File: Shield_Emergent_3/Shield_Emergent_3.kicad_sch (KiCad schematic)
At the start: 17 parts, among them J1 USB3_B_Micro, J2 Conn_02x04_Odd_Even, J3 USB3_B_Micro, U3 SP3012-06UTG, U4 SP3012-06UTG, X1 USB_C_24pins

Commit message: v1.1 Geometry was established, LF routing was completed
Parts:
- removed J2: Conn_02x04_Odd_Even, Connector_PinHeader_2.54mm:PinHeader_2x04_P2.54mm_Vertical, symbol Connector_Generic:Conn_02x04_Odd_Even
- added J2: Conn_02x03_Odd_Even, Connector_PinSocket_2.54mm:PinSocket_2x03_P2.54mm_Vertical, symbol Connector_Generic:Conn_02x03_Odd_Even
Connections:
- net BTN1: now also J2.5 (Pin_5)
- net BTN2: now also J2.6 (Pin_6)
- net EN1: now also J2.1 (Pin_1)
- net EN2: now also J2.2 (Pin_2)
- net nFLT1: now also J2.3 (Pin_3)
- net nFLT2: now also J2.4 (Pin_4)
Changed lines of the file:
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@@
 	(wire
 		(pts
-			(xy 50.8 33.02) (xy 52.07 33.02)
-		)
-		(stroke
-			(width 0)
-			(type default)
-		)
-	)
-	(wire
-		(pts
 			(xy 234.95 53.34) (xy 236.22 53.34)
 		)
@@
 	(wire
 		(pts
-			(xy 36.83 33.02) (xy 38.1 33.02)
-		)
-		(stroke
-			(width 0)
-			(type default)
-		)
-	)
-	(wire
-		(pts
 			(xy 66.04 67.31) (xy 68.58 67.31)
 		)
@@
 		)
 	)
-	(global_label "VOUT2"
-		(shape input)
-		(at 52.07 33.02 0)
-		(fields_autoplaced yes)
-		(effects
-			(font
-				(size 1.27 1.27)
-			)
-			(justify left)
-		)
-		(property "Intersheetrefs" "${INTERSHEET_REFS}"
-			(at 60.9819 33.02 0)
-			(effects
-				(font
-					(size 1.27 1.27)
-				)
-				(justify left)
-				(hide yes)
-			)
-		)
-	)
 	(global_label "RX2+"
 		(shape input)
@@
 		)
 	)
-	(global_label "VOUT1"
-		(shape input)
-		(at 36.83 33.02 180)
-		(fields_autoplaced yes)
-		(effects
-			(font
-				(size 1.27 1.27)
-			)
-			(justify right)
-		)
-		(property "Intersheetrefs" "${INTERSHEET_REFS}"
-			(at 27.9181 33.02 0)
-			(effects
-				(font
-					(size 1.27 1.27)
-				)
-				(justify right)
-				(hide yes)
-			)
-		)
-	)
 	(global_label "RX1+"
 		(shape input)
@@
 	)
 	(symbol
-		(lib_id "Connector_Generic:Conn_02x04_Odd_Even")
-		(at 43.18 35.56 0)
-		(unit 1)
-		(exclude_from_sim no)
-		(in_bom yes)
-		(on_board yes)
-		(dnp no)
-		(fields_autoplaced yes)
-		(property "Reference" "J2"
-			(at 44.45 29.21 0)
-			(effects
-				(font
-					(size 1.27 1.27)
-				)
-			)
-		)
-		(property "Value" "Conn_02x04_Odd_Even"
-			(at 44.45 29.21 0)
-			(effects
-				(font
-					(size 1.27 1.27)
-				)
-				(hide yes)
-			)
-		)
-		(property "Footprint" "Connector_PinHeader_2.54mm:PinHeader_2x04_P2.54mm_Vertical"
-			(at 43.18 35.56 0)
-			(effects
-				(font
-					(size 1.27 1.27)
-				)
-				(hide yes)
-			)
-		)
-		(property "Datasheet" "~"
-			(at 43.18 35.56 0)
-			(effects
-				(font
-					(size 1.27 1.27)
-				)
-				(hide yes)
-			)
-		)
-		(property "Description" "Generic connector, double row, 02x04, odd/even pin numbering scheme (row 1 odd numbers, row 2 even numbers), script generated (kicad-library-utils/schlib/autogen/connector/)"
-			(at 43.18 35.56 0)
-			(effects
-				(font
-					(size 1.27 1.27)
-				)
-				(hide yes)
-			)
-		)
-		(pin "7"
-		)
-		(pin "2"
-		)
-		(pin "4"
-		)
-		(pin "1"
-		)
-		(pin "6"
-		)
-		(pin "3"
-		)
-		(pin "5"
-		)
-		(pin "8"
-		)
-		(instances
-			(project "Shield_Emergent_3"
-				(path "/e876a9d6-39c5-4a0a-9fdb-4afd596a6b67"
-					(reference "J2")
-					(unit 1)
-				)
-			)
-		)
-	)
-	(symbol
 		(lib_id "power:VBUS")
 		(at 33.02 53.34 0)
@@
 					(unit 1)
 				)
+			)
+		)
+	)
+	(symbol
+		(lib_id "Connector_Generic:Conn_02x03_Odd_Even")
+		(at 43.18 38.1 0)
+		(unit 1)
+		(exclude_from_sim no)
+		(in_bom yes)
+		(on_board yes)
+		(dnp no)
+		(fields_autoplaced yes)
+		(property "Reference" "J2"
+			(at 44.45 31.75 0)
+			(effects
+				(font
+					(size 1.27 1.27)
+				)
+			)
+		)
+		(property "Value" "Conn_02x03_Odd_Even"
+			(at 44.45 31.75 0)
+			(effects
+				(font
+					(size 1.27 1.27)
+				)
+				(hide yes)
+			)
+		)
+		(property "Footprint" "Connector_PinSocket_2.54mm:PinSocket_2x03_P2.54mm_Vertical"
+			(at 43.18 38.1 0)
+			(effects
+				(font
+					(size 1.27 1.27)
+				)
+				(hide yes)
+			)
+		)
+		(property "Datasheet" "~"
+			(at 43.18 38.1 0)
+			(effects
+				(font
+					(size 1.27 1.27)
+				)
+				(hide yes)
+			)
+		)
+		(property "Description" "Generic connector, double row, 02x03, odd/even pin numbering scheme (row 1 odd numbers, row 2 even numbers), script generated (kicad-library-utils/schlib/autogen/connector/)"
+			(at 43.18 38.1 0)
+			(effects
+				(font
+					(size 1.27 1.27)
+				)
+				(hide yes)
+			)
+		)
+		(pin "2"
+		)
+		(pin "3"
+		)
+		(pin "4"
+		)
+		(pin "5"
+		)
+		(pin "6"
+		)
+		(pin "1"
+		)
+		(instances
+			(project "Shield_Emergent_3"
+				(path "/e876a9d6-39c5-4a0a-9fdb-4afd596a6b67"
+					(reference "J2")
+					(unit 1)
+				)

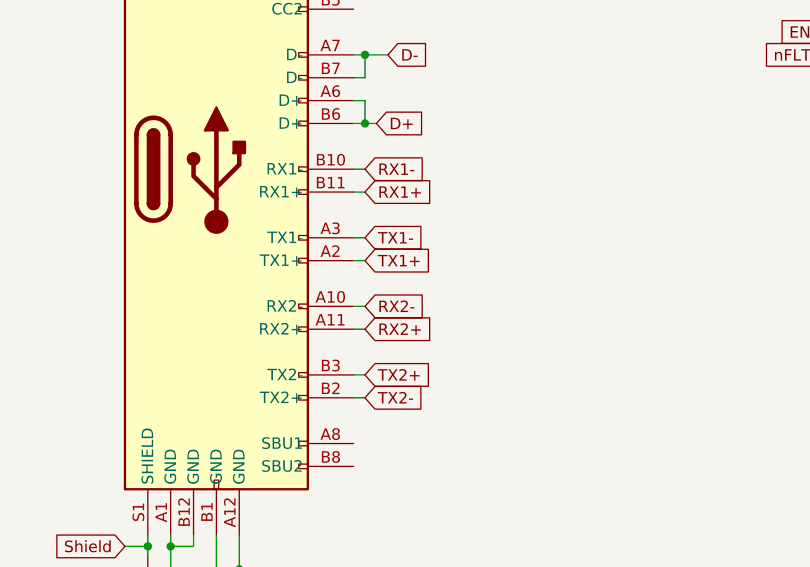
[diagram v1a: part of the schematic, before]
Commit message: v1.3 draft routing was completed
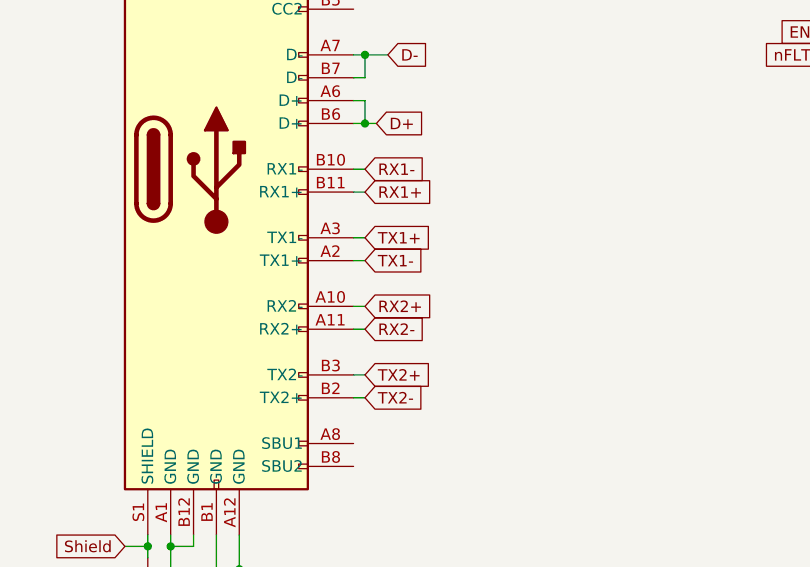
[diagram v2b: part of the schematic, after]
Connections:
- net RX2+: now also X1.A10 (RX2-); no longer X1.A11 (RX2+)
- net RX2-: now also X1.A11 (RX2+); no longer X1.A10 (RX2-)
- net TX1+: now also X1.A3 (TX1-); no longer X1.A2 (TX1+)
- net TX1-: now also X1.A2 (TX1+); no longer X1.A3 (TX1-)

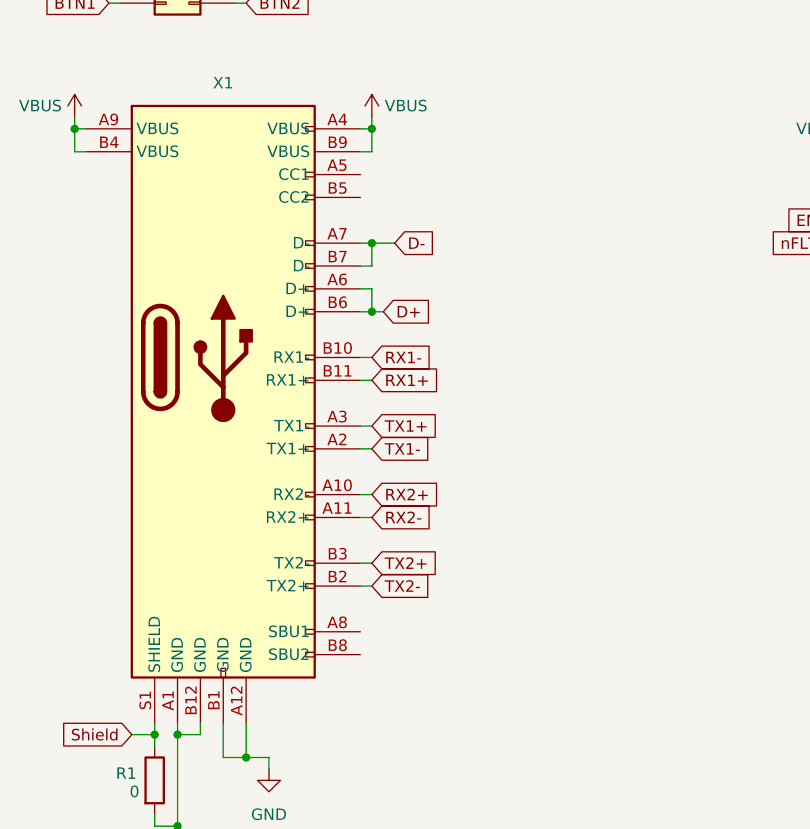
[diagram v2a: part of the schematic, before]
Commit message: v1.4  draft ruting was totally completed.
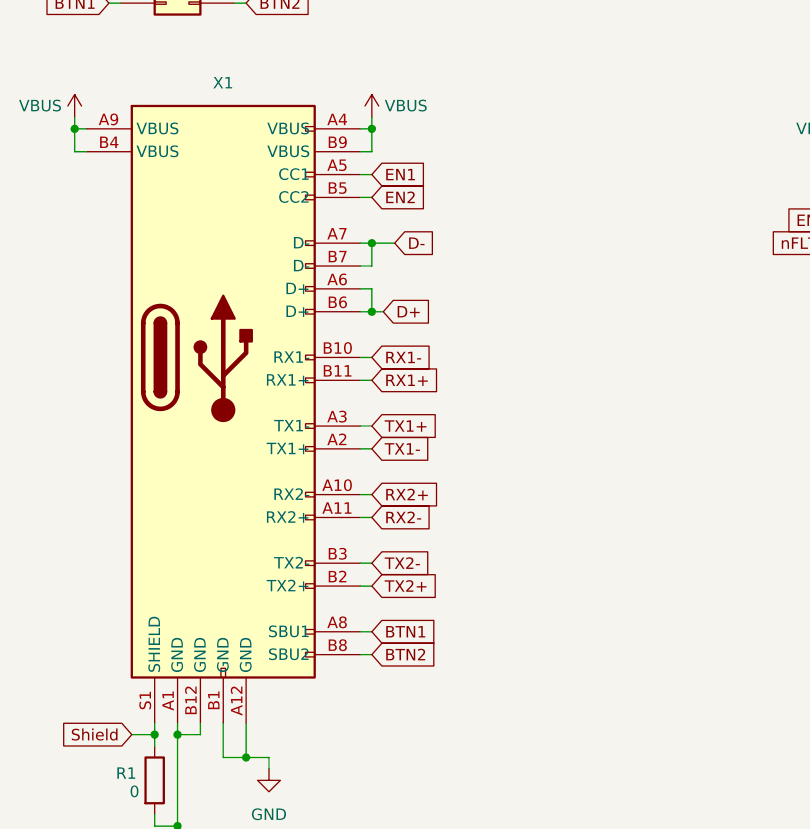
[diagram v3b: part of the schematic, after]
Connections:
- net BTN1: now also X1.A8 (SBU1)
- net BTN2: now also X1.B8 (SBU2)
- net EN1: now also X1.A5 (CC1)
- net EN2: now also X1.B5 (CC2)
- net TX2+: now also X1.B2 (TX2+); no longer X1.B3 (TX2-)
- net TX2-: now also X1.B3 (TX2-); no longer X1.B2 (TX2+)

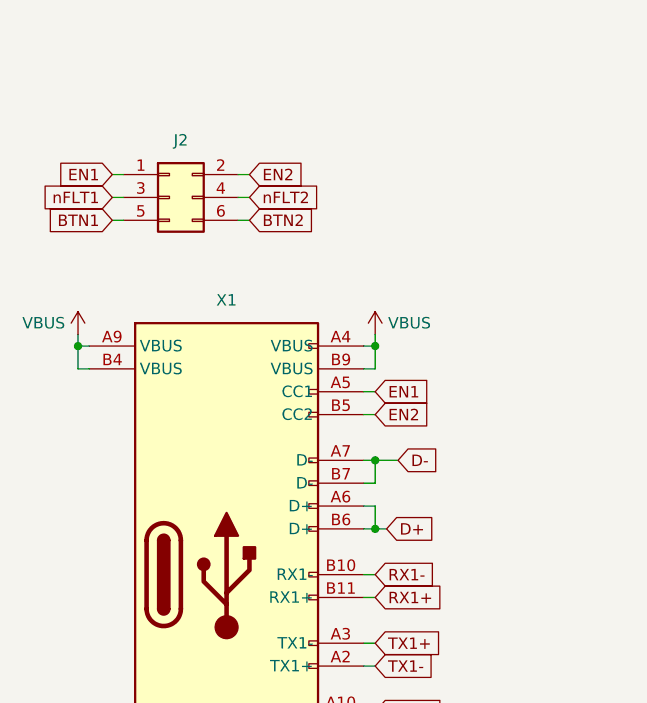
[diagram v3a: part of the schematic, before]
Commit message: v1.6 routing is nearly completed
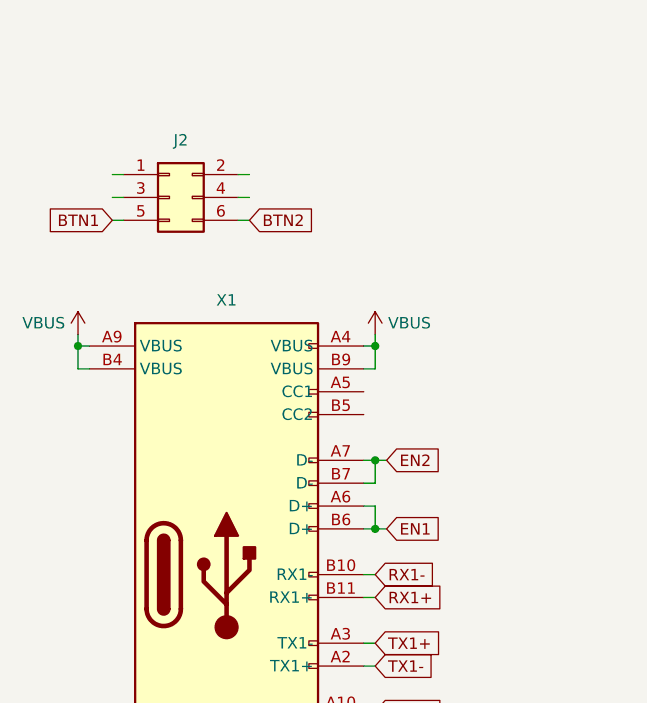
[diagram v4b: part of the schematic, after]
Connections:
- net D+: no longer X1.A6 (D+), X1.B6 (D+)
- net D-: no longer X1.A7 (D-), X1.B7 (D-)
- net EN1: now also X1.A6 (D+), X1.B6 (D+); no longer J2.1 (Pin_1), X1.A5 (CC1)
- net EN2: now also X1.A7 (D-), X1.B7 (D-); no longer J2.2 (Pin_2), X1.B5 (CC2)
- net nFLT1: no longer J2.3 (Pin_3)
- net nFLT2: no longer J2.4 (Pin_4)

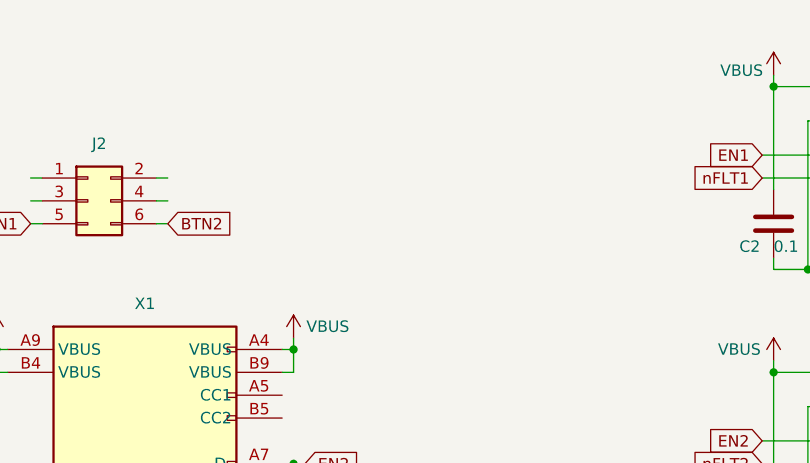
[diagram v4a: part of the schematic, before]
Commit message: v1.7 Keyboard connector was added, decomposed and routed
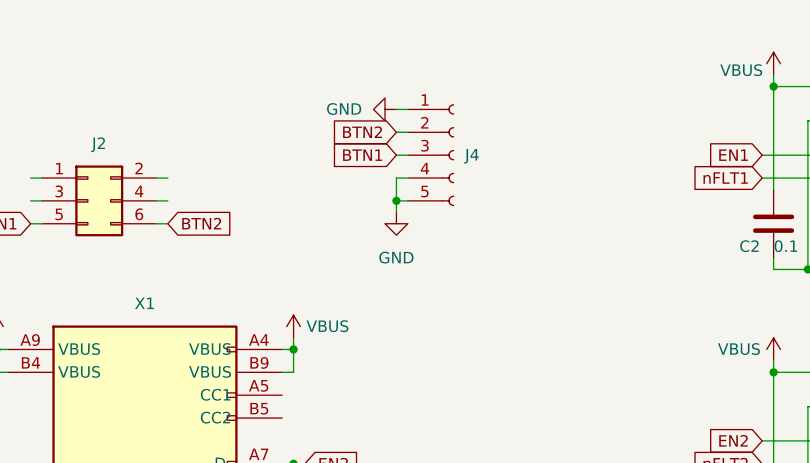
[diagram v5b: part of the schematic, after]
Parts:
- added J4: Conn_01x05_Socket, myLib8:04FFS-SP-TF (LF)(SN), symbol Connector:Conn_01x05_Socket
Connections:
- net BTN1: now also J4.3 (Pin_3)
- net BTN2: now also J4.2 (Pin_2)
- net GND: now also J4.1 (Pin_1), J4.4 (Pin_4), J4.5 (Pin_5)

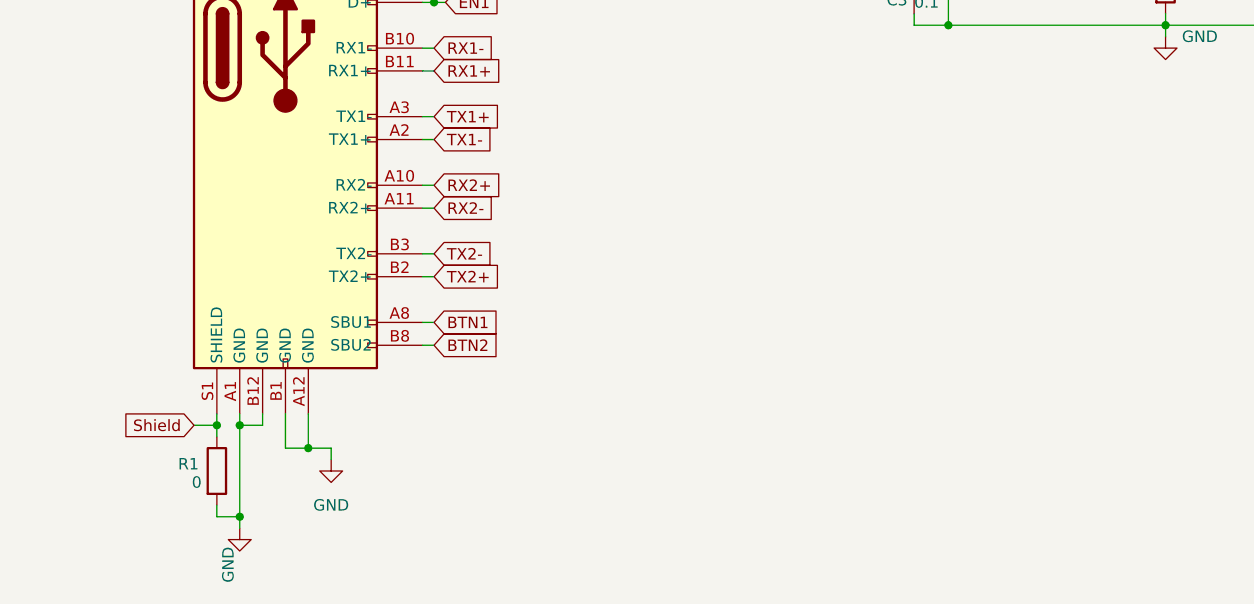
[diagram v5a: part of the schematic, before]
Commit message: v1.8 ESD protection 4 buttons was added
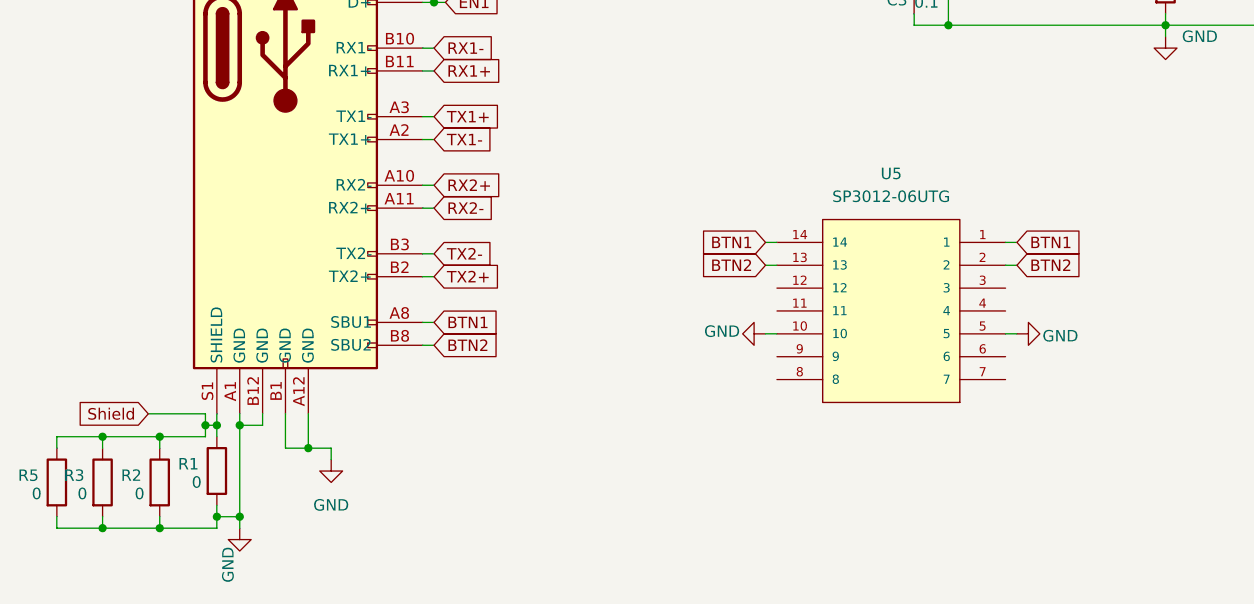
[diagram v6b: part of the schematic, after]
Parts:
- added R2, R3, R5: 0, Resistor_SMD:R_0402_1005Metric, symbol Device:R
- added U5: SP3012-06UTG, myLib8:DFN-14_1.35x3.5mm_P0.5mm, symbol myLib8:SP3012-06UTG
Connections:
- net BTN1: now also U5.1, U5.14
- net BTN2: now also U5.13, U5.2
- net GND: now also R2.2, R3.2, R5.2, U5.10, U5.5
- net Shield: now also R2.1, R3.1, R5.1
